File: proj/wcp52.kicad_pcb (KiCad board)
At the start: 4 copper layers, 100 x 100 mm, 310 parts, among them J1 MicroUSB-B, J2 IN1, J3 IN2, J4 OUT, J5 CONN-PJ-037A, J6 JLINK, Q1 MMBT3906, Q10 MMBT3904, Q11 BFR540, Q12 BFR540, Q13 MMBT3904, Q14 MMBT3904, Q15 MMBT3904, Q16 MMBT3904, Q17 PZT2907A, Q18 PZT2907A, Q19 MMBT3904, Q2 IRLML6402, Q3 AOD417, Q4 MMBT3906, Q5 2N7002, Q6 2N7002, Q7 MMBT3906, Q8 2N7002, Q9 2N7002, U1 TL431AIDBZ, U10 MASWSS0162, U11 AD8310ARMZ, U12 ATSAM4S16CA-AU, U13 FT230XS_DNP, U14 L78M05CDT, U15 MC79M05CDT, U16 AZ1117CH-1.8TRG1, U17 MCP1700T-vv02E/TT, U2 LM393M, U3 LMH6714MF, U4 AD9958BCPZ, U5 LMH6714MF, U6 AD8000YRDZ, U7 THS3001IDGN, U8 MAADSS0008, U9 MASWSS0162, X1 25 MHz, X2 12MHz

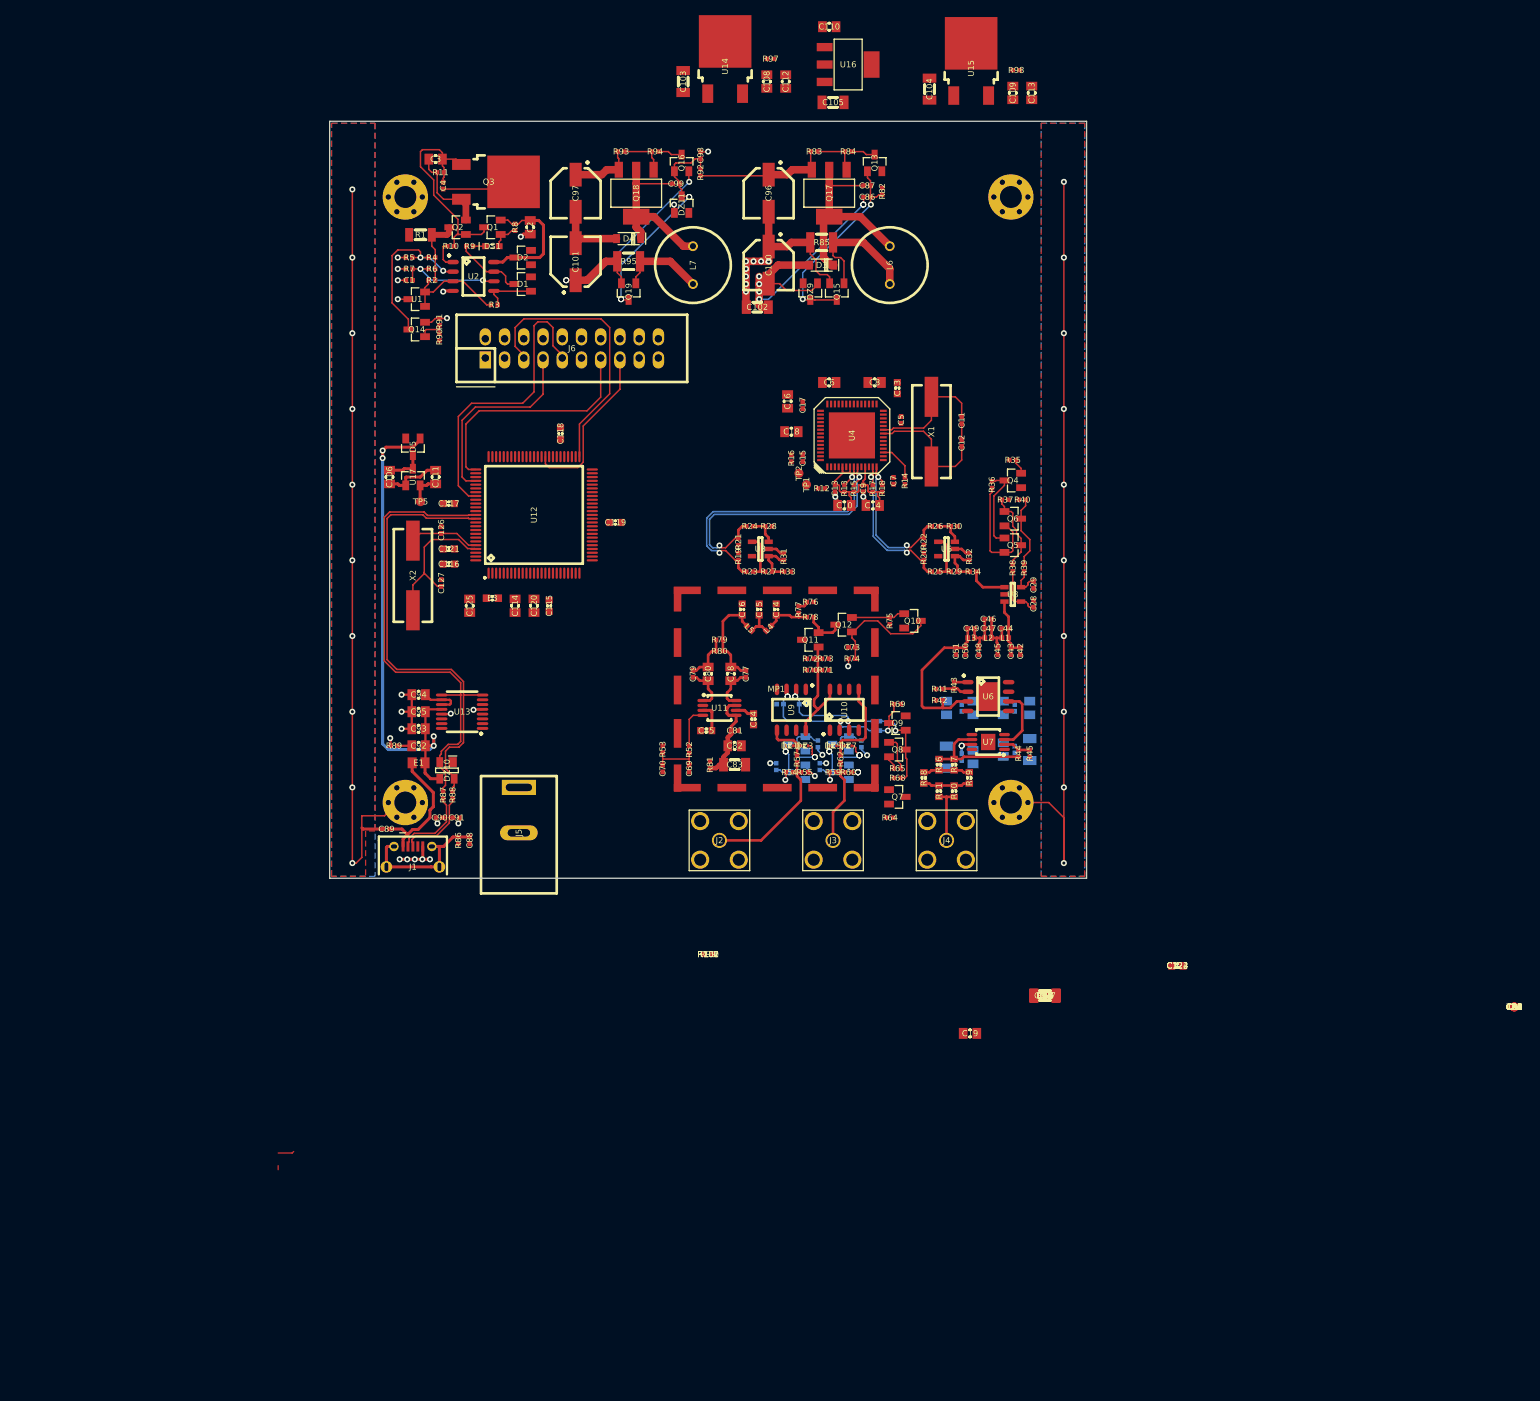
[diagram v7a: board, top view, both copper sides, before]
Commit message: All parts placed
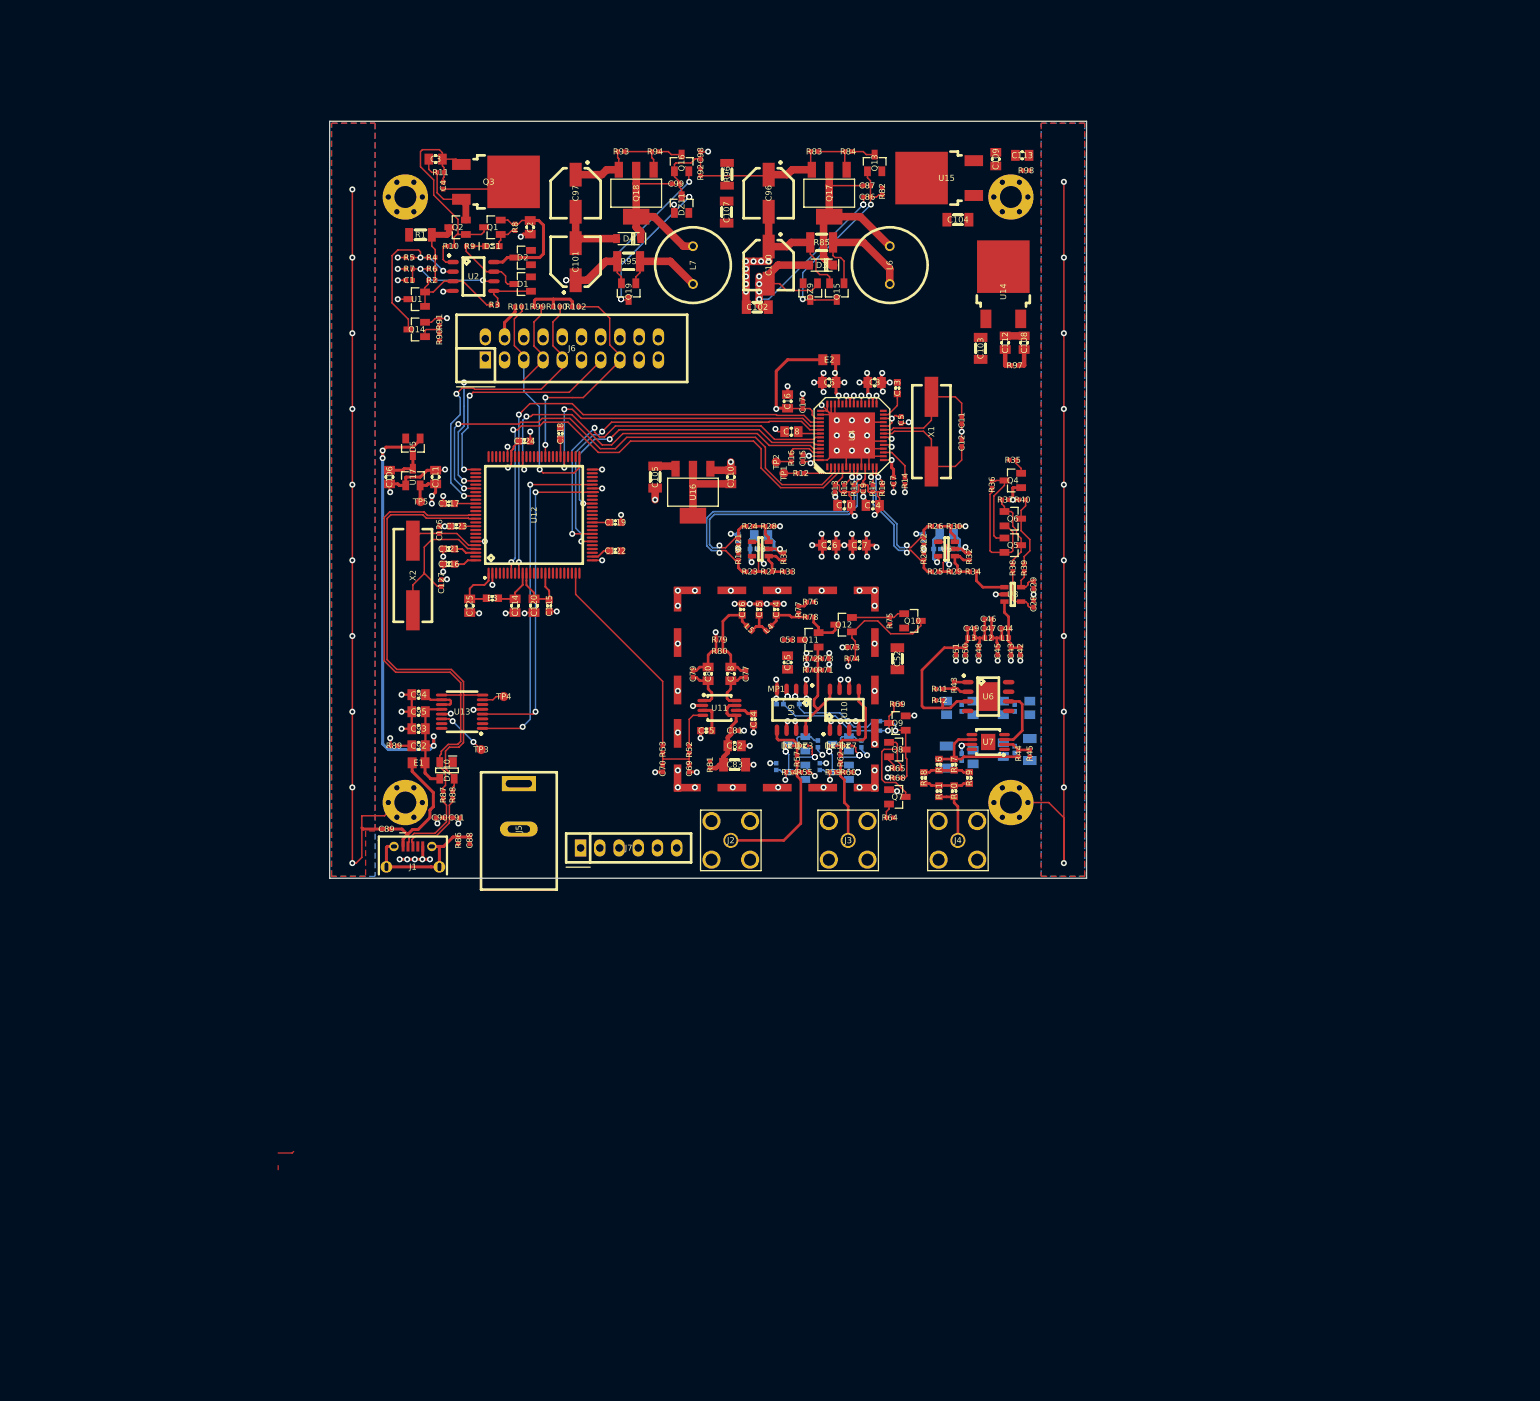
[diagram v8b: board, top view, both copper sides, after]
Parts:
- removed C54, C55, C56, C57, C58, C59, C60, C61, C62: 1n, IPC7351-Nominal:CAPC1005X55
- removed C63, C64, C66, C67, C68: 220n, IPC7351-Nominal:CAPC2012X70
- added C128: 1n, IPC7351-Nominal:CAPC1005X55, B.Cu at (129.0, 80.0)
- added C129: 1n, IPC7351-Nominal:CAPC1005X55, B.Cu at (153.5, 80.0)
- added J7: AUX, conn-100mil:CONN-100MIL-F-1x6, F.Cu at (114.5, 121.0)
- C19, C20, C21, C22, C24, C25: moved to B.Cu
- moved TP3 140.7 mm to (95.0, 108.0)
- moved TP4 139.7 mm to (98.0, 101.0)
- moved C20 117.3 mm to (131.0, 81.5)
- moved R96 116.3 mm to (127.5, 32.0), turned to 270 degrees
- moved C21 115.4 mm to (133.2, 81.5)
- moved C107 111.7 mm to (127.5, 37.0), turned to 270 degrees
- moved C123 111.5 mm to (91.8, 78.5), turned to 180 degrees
- moved C124 110.6 mm to (100.8, 67.2)
- moved C53 107.6 mm to (135.5, 93.5), turned to 180 degrees
- moved C24 97.3 mm to (155.2, 81.5)
- moved C25 95.4 mm to (157.8, 81.5)
- moved C122 92.3 mm to (112.8, 81.8)
- moved R101 89.1 mm to (100.0, 49.5), turned to 180 degrees
- moved E2 88.7 mm to (141.0, 56.5)
- moved R99 88.5 mm to (102.5, 49.5)
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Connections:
- R53 pad 1: /InputFrontend/OUT -> /MPU/ADIN
- R64 pad 1: /InputFrontend/INPUTSEL -> /MPU/CHANSEL
- U12 pad 24: Net-(U12-Pad24) -> /MPU/ADIN
- U12 pad 31: Net-(U12-Pad31) -> /Synth/SCLK
- U12 pad 33: Net-(U12-Pad33) -> /Synth/SDI
- U12 pad 41: Net-(U12-Pad41) -> /Synth/SDO
- U12 pad 55: Net-(U12-Pad55) -> /Synth/#CS
- U12 pad 66: Net-(U12-Pad66) -> /Synth/SYNC_IO
- U12 pad 67: Net-(U12-Pad67) -> /MPU/CHANSEL
- U12 pad 7: Net-(U12-Pad7) -> /Synth/PWR_DWN_CTL
- U12 pad 81: Net-(U12-Pad81) -> /Synth/MASTER_RESET
- U12 pad 9: Net-(U12-Pad9) -> /Synth/IO_UPDATE
- U4 pad 50: /Synth/SDIO_0 -> /Synth/SDI
- U4 pad 52: /Synth/SDIO_2 -> /Synth/SDO
- U4 pad 53: /Synth/SDIO_3 -> /Synth/SYNC_IO
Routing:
- net GND: track 306.3 -> 515.8 mm, vias 59 -> 176
- net /Synth/PWR_DWN_CTL: track 0.00 -> 70.6 mm, vias 0 -> 2
- net /Synth/MASTER_RESET: track 0.00 -> 68.7 mm, vias 0 -> 2
- net /Synth/IO_UPDATE: track 0.00 -> 62.4 mm, vias 0 -> 2
- net /Synth/SYNC_IO: track 0.00 -> 51.1 mm, vias 0 -> 2
- net /Synth/SDI: track 0.00 -> 50.0 mm, vias 0 -> 2
- net /Synth/SCLK: track 0.00 -> 48.0 mm, vias 0 -> 2
- net /Comm/SER_FROMUSB: track 0.00 -> 46.0 mm, vias 0 -> 2
- net /MPU/SER_FROM_MPU: track 0.00 -> 45.2 mm, vias 0 -> 2
- net /Synth/#CS: track 0.00 -> 43.9 mm, vias 0 -> 2
- net /Synth/SDO: track 0.00 -> 41.9 mm, vias 0 -> 2
- net +1.8A: track 20.1 -> 58.8 mm, vias 0 -> 18
- net +1.8: track 0.00 -> 32.3 mm, vias 0 -> 2
- net +3.3SB: track 4.30 -> 33.7 mm, vias 0 -> 4
- net /MPU/ADIN: track 0.00 -> 27.6 mm
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- added copper zone on In1.Cu, net +1.8A
- added copper zone on In1.Cu, net +3.3SB
